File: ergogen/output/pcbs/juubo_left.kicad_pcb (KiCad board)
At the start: 2 copper layers, 145.6 x 125.5 mm, 50 parts

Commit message: Adjust holes
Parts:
- moved _3 19.1 mm to (109.5, 86.7)
- moved _6 15.2 mm to (166.7, 85.5)
- moved _4 12.0 mm to (184.6, 120.5)
- moved _5 10.3 mm to (206.8, 139.9)
- moved T1 0.23 mm to (199.2, 50.4)
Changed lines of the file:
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@@
       )
         (module E73:SPDT_C128955 (layer F.Cu)
-            (at 199.25 50.18000000000001 0)
+            (at 199.25 50.410500000000006 0)
             (fp_text reference "T1" (at 0 0) (layer F.SilkS) hide (effects (font (size 1.27 1.27) (thickness 0.15))))
             (fp_text value "" (at 0 0) (layer F.SilkS) hide (effects (font (size 1.27 1.27) (thickness 0.15))))
@@
     )
     (module "MountingHole_2.2mm_M2_Pad_Via" (version 20210722) (generator pcbnew) (layer "F.Cu")
-      (at 109.525 105.715 0)
+      (at 109.525 86.66499999999999 0)
       (fp_text reference "_3" (at 0 -3.2) (layer "F.SilkS") hide
         (effects (font (size 1 1) (thickness 0.15)))
@@
     )
     (module "MountingHole_2.2mm_M2_Pad_Via" (version 20210722) (generator pcbnew) (layer "F.Cu")
-      (at 177.92129269999998 130.5355175 -15)
+      (at 184.5597717 120.4810859 -15)
       (fp_text reference "_4" (at 0 -3.2) (layer "F.SilkS") hide
         (effects (font (size 1 1) (thickness 0.15)))
@@
     )
     (module "MountingHole_2.2mm_M2_Pad_Via" (version 20210722) (generator pcbnew) (layer "F.Cu")
-      (at 202.77889639999995 149.2843828 -135)
+      (at 206.82001159999996 139.8551139 -135)
       (fp_text reference "_5" (at 0 -3.2) (layer "F.SilkS") hide
         (effects (font (size 1 1) (thickness 0.15)))
@@
     )
     (module "MountingHole_2.2mm_M2_Pad_Via" (version 20210722) (generator pcbnew) (layer "F.Cu")
-      (at 166.675 100.715 0)
+      (at 166.675 85.475 0)
       (fp_text reference "_6" (at 0 -3.2) (layer "F.SilkS") hide
         (effects (font (size 1 1) (thickness 0.15)))

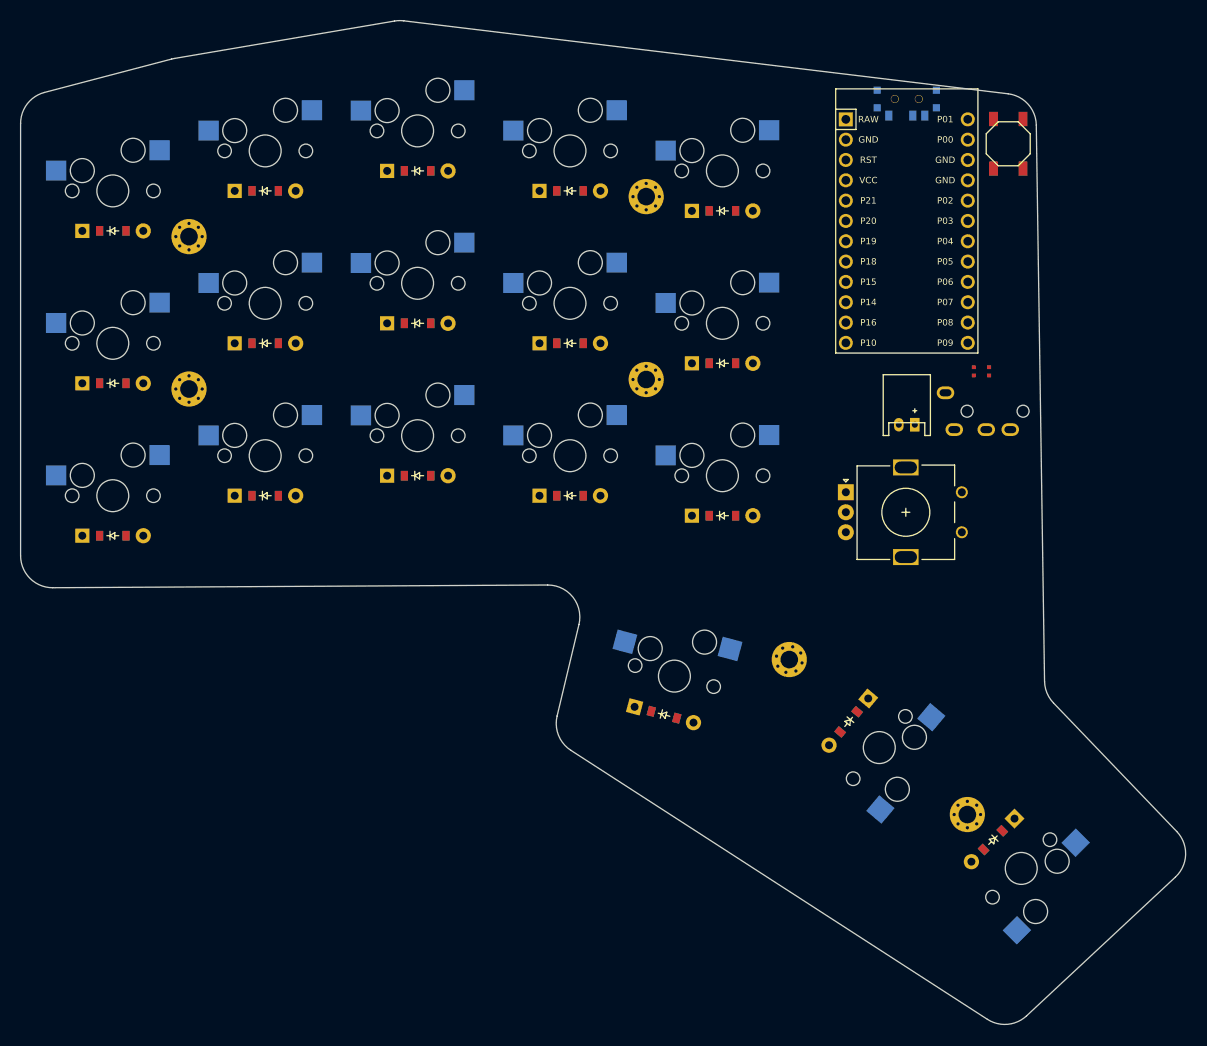
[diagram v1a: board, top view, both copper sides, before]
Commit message: Heighten case wall & plate thickness, left side
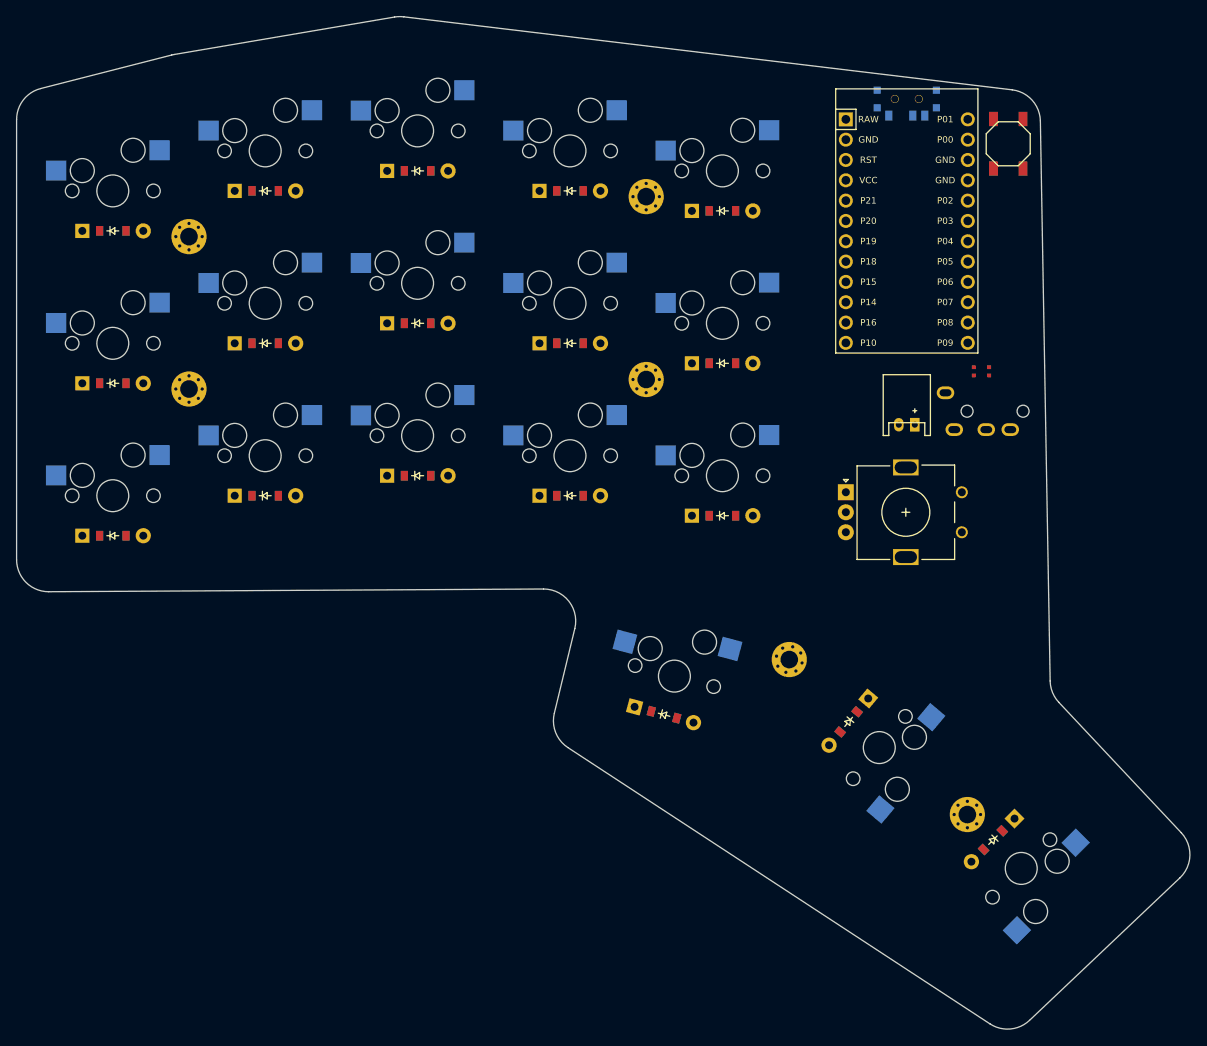
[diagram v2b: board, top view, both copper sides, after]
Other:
- board size 145.6 x 125.5 mm -> 146.7 x 126.6 mm
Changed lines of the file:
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@@
       (pad "1" thru_hole circle locked (at 0 -1.65) (size 0.7 0.7) (drill 0.4) (layers *.Cu *.Mask))
     )
-            (gr_line (start 88.475 107.50296162142857) (end 88.475 53.46061479002625) (angle 90) (layer Edge.Cuts) (width 0.15))
-(gr_line (start 91.45952643622041 49.591659728026144) (end 107.35403904220854 45.419871642464955) (angle 90) (layer Edge.Cuts) (width 0.15))
-(gr_line (start 107.69925258946857 45.34538260727286) (end 135.22213637456363 40.667368578713194) (angle 90) (layer Edge.Cuts) (width 0.15))
-(gr_line (start 136.3718892001102 40.63965580114411) (end 211.91679227467918 49.76123537830968) (angle 90) (layer Edge.Cuts) (width 0.15))
-(gr_line (start 215.43685866268356 53.67301305311594) (end 216.46896193090296 123.19177812522139) (angle 90) (layer Edge.Cuts) (width 0.15))
-(gr_line (start 217.5814403821686 125.90093007325962) (end 232.9929319765313 141.97234609192535) (angle 90) (layer Edge.Cuts) (width 0.15))
-(gr_line (start 232.83356967389372 147.6665484861759) (end 214.22282445150165 165.01808035980326) (angle 90) (layer Edge.Cuts) (width 0.15))
-(gr_line (start 209.32507655838322 165.45261328126142) (end 157.25771111513586 131.8273611550128) (angle 90) (layer Edge.Cuts) (width 0.15))
-(gr_line (start 155.53717774253036 127.53789858189975) (end 158.27097555791937 116.09220110959882) (angle 90) (layer Edge.Cuts) (width 0.15))
-(gr_line (start 154.35843513532046 111.16300310365209) (end 92.49697760000302 111.50290122197801) (angle 90) (layer Edge.Cuts) (width 0.15))
-(gr_arc (start 92.475 53.46061479002625) (end 91.45952639999999 49.59165969002625) (angle -75.29345756940775) (layer Edge.Cuts) (width 0.15))
-(gr_arc (start 108.36951260598812 49.288826704465066) (end 107.69925260598812 45.345382604465065) (angle -5.060269060893688) (layer Edge.Cuts) (width 0.15))
-(gr_arc (start 135.8923963910832 44.610812675905386) (end 136.3718891910832 40.63965587590538) (angle -16.53105809028341) (layer Edge.Cuts) (width 0.15))
-(gr_arc (start 211.43729946565222 53.73239225307096) (end 215.4368586656522 53.67301305307096) (angle -82.26463964139997) (layer Edge.Cuts) (width 0.15))
-(gr_arc (start 220.46852112793434 123.1323989252669) (end 216.46896192793434 123.1917781252669) (angle -42.9485999083563) (layer Edge.Cuts) (width 0.15))
-(gr_arc (start 230.10585123076567 144.74087723991798) (end 232.83356963076565 147.666548439918) (angle -90.80456151683016) (layer Edge.Cuts) (width 0.15))
-(gr_arc (start 211.4951060083736 162.09240911354533) (end 209.3250765083736 165.45261331354533) (angle -75.84910373357374) (layer Edge.Cuts) (width 0.15))
-(gr_arc (start 159.42774056512627 128.46715698729673) (end 155.53717776512627 127.53789858729674) (angle -70.5788905873116) (layer Edge.Cuts) (width 0.15))
-(gr_arc (start 154.38041273532352 115.16294270420167) (end 158.27097553532352 116.09220110420166) (angle -103.74818780803423) (layer Edge.Cuts) (width 0.15))
-(gr_arc (start 92.475 107.50296162142857) (end 88.475 107.50296162142857) (angle -90.3148075166796) (layer Edge.Cuts) (width 0.15))
+            (gr_line (start 87.975 108.00296162142857) (end 87.975 52.98073082915602) (angle 90) (layer Edge.Cuts) (width 0.15))
+(gr_line (start 90.98388315812895 49.10546466544017) (end 107.36597127301164 44.91567230869268) (angle 90) (layer Edge.Cuts) (width 0.15))
+(gr_line (start 107.68682809836312 44.84749437521633) (end 135.22363254175121 40.16711427792308) (angle 90) (layer Edge.Cuts) (width 0.15))
+(gr_line (start 136.37043416110947 40.13904635145789) (end 212.4231066866209 49.26460738242512) (angle 90) (layer Edge.Cuts) (width 0.15))
+(gr_line (start 215.9459537820649 53.166192607861376) (end 217.1697567052548 123.16041708043849) (angle 90) (layer Edge.Cuts) (width 0.15))
+(gr_line (start 218.25322385991927 125.82862862927247) (end 233.55760394433358 142.12669744297853) (angle 90) (layer Edge.Cuts) (width 0.15))
+(gr_line (start 233.39277670610832 147.76853689018037) (end 214.59261460229058 165.5806373433828) (angle 90) (layer Edge.Cuts) (width 0.15))
+(gr_line (start 209.65071306689939 166.02363068906197) (end 156.8864930261346 131.48320920349795) (angle 90) (layer Edge.Cuts) (width 0.15))
+(gr_line (start 155.18951070488046 127.1957211694695) (end 157.752610618467 116.6038219609112) (angle 90) (layer Edge.Cuts) (width 0.15))
+(gr_line (start 153.84284346721205 111.66308877215818) (end 91.99697760000304 112.00290122197801) (angle 90) (layer Edge.Cuts) (width 0.15))
+(gr_arc (start 91.975 52.98073082915602) (end 90.9838832 49.105464729156026) (angle -75.65386407377886) (layer Edge.Cuts) (width 0.15))
+(gr_arc (start 108.35708811488269 48.79093847240853) (end 107.68682811488269 44.847494372408526) (angle -4.699862556522419) (layer Edge.Cuts) (width 0.15))
+(gr_arc (start 135.89389255827078 44.110558375115275) (end 136.37043415827077 40.13904627511528) (angle -16.488480181302705) (layer Edge.Cuts) (width 0.15))
+(gr_arc (start 211.94656508378222 53.2361194060825) (end 215.94595378378222 53.166192606082504) (angle -82.15611455141583) (layer Edge.Cuts) (width 0.15))
+(gr_arc (start 221.16914540353744 123.0904902822167) (end 217.16975670353744 123.16041708221671) (angle -42.19733729001143) (layer Edge.Cuts) (width 0.15))
+(gr_arc (start 230.64168240071479 144.8648357900348) (end 233.3927767007148 147.7685368900348) (angle -89.744890333001) (layer Edge.Cuts) (width 0.15))
+(gr_arc (start 211.84152029689707 162.67693624323724) (end 209.65071309689708 166.02363064323723) (angle -76.66361533542084) (layer Edge.Cuts) (width 0.15))
+(gr_arc (start 159.07730025613233 128.1365147576732) (end 155.18951075613234 127.1957211576732) (angle -70.39382807020911) (layer Edge.Cuts) (width 0.15))
+(gr_arc (start 153.86482106721508 115.66302837270769) (end 157.75261056721507 116.60382197270769) (angle -103.91812532830821) (layer Edge.Cuts) (width 0.15))
+(gr_arc (start 91.975 108.00296162142857) (end 87.975 108.00296162142857) (angle -90.31480751667982) (layer Edge.Cuts) (width 0.15))
 )
